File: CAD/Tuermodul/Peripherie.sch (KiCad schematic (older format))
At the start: 63 parts, among them J201 Conn_02x20_Odd_Even, Q205 Q_NPN_CBE, Q206 Q_NPN_CBE, Q207 Q_NPN_CBE, Q208 Q_NPN_CBE, Q209 Q_PMOS_GDS, Q210 Q_PMOS_GDS, Q211 Q_PMOS_GDS, Q212 Q_PMOS_GDS, Q213 Q_NPN_CBE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

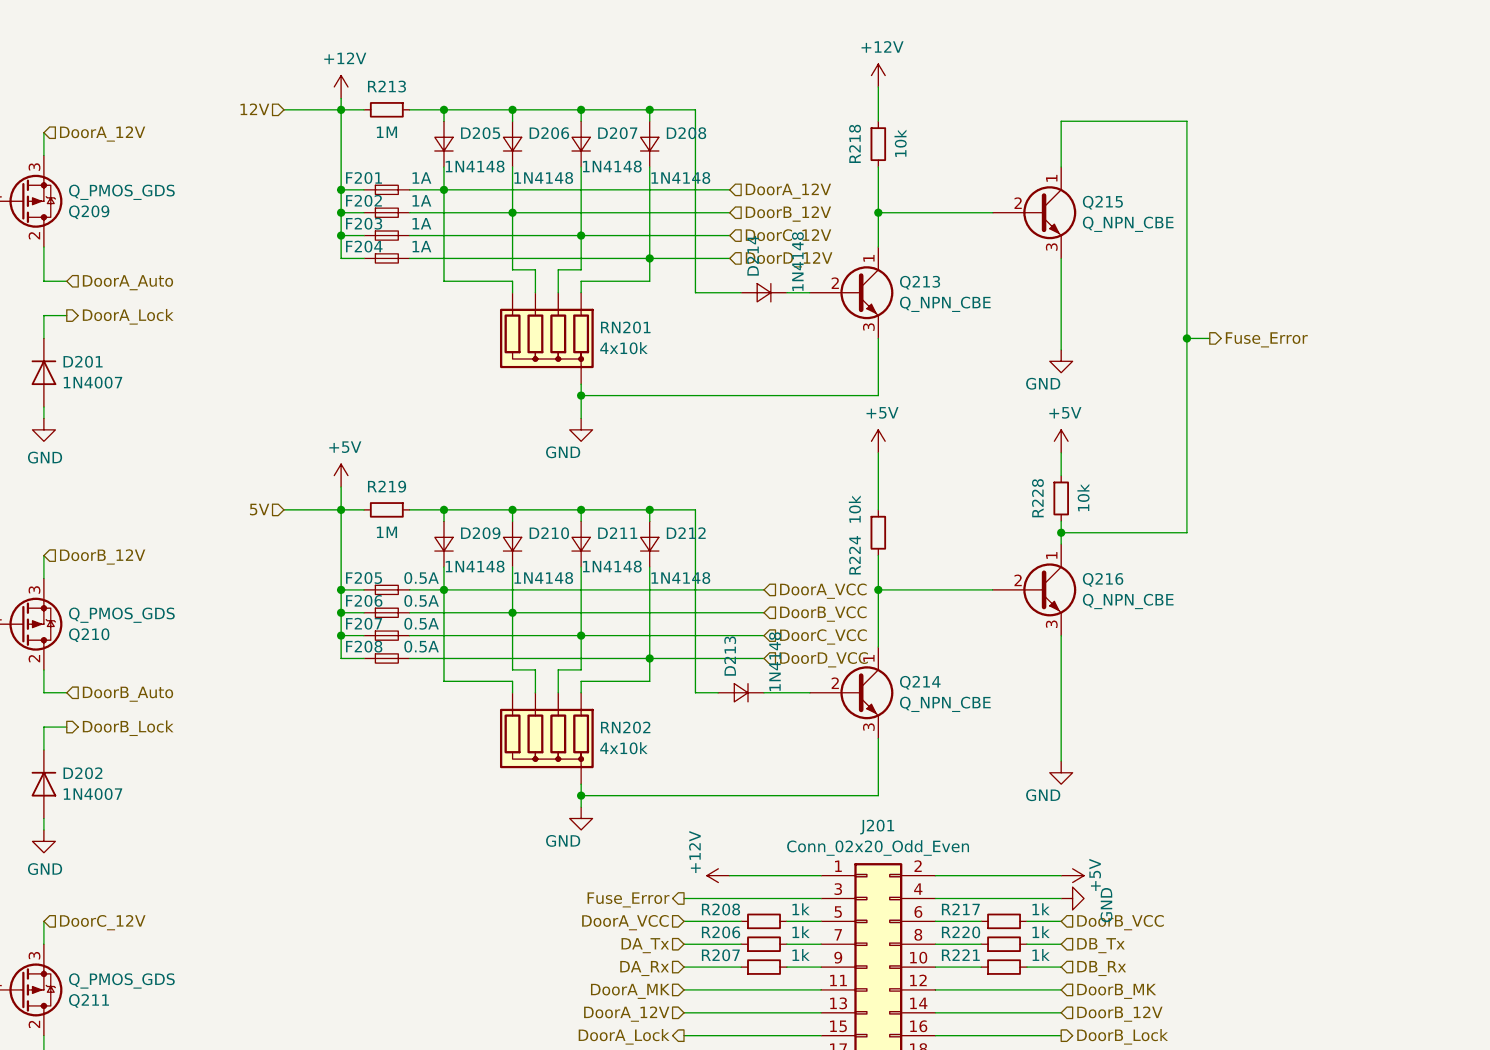
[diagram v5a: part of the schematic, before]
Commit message: -mod: Änderungen aus Review in Schaltplan und Layout
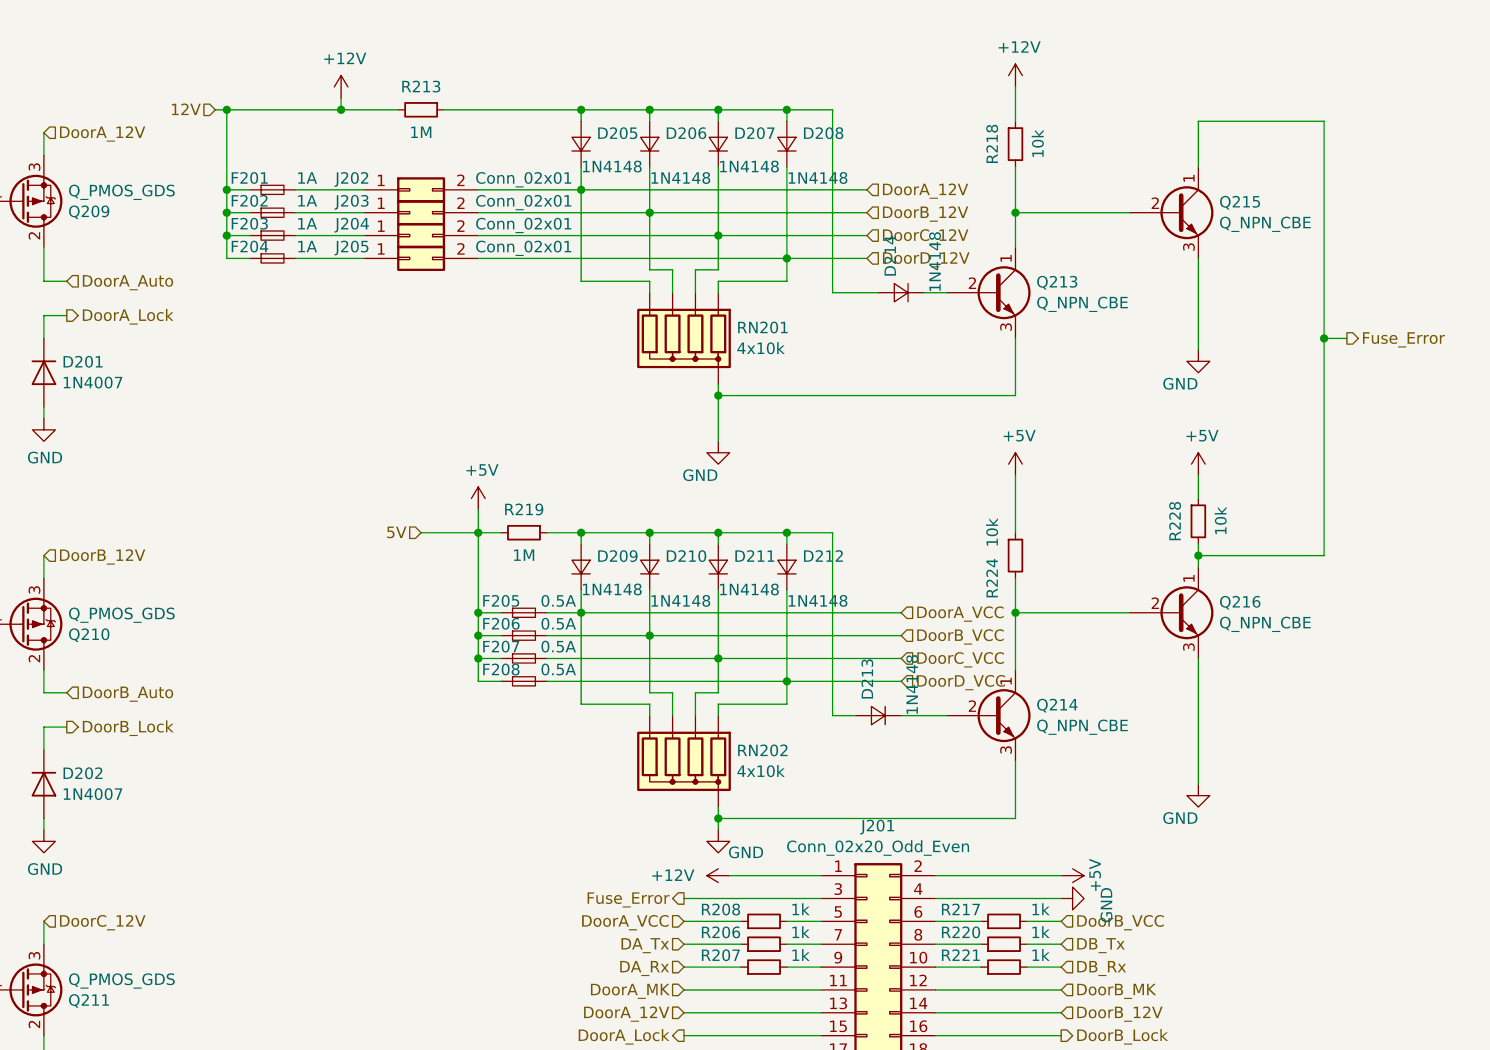
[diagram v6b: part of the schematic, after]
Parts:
- added J202, J203, J204, J205: Conn_02x01, Connector_PinHeader_2.54mm:PinHeader_2x01_P2.54mm_Vertical, symbol Connector_Generic:Conn_02x01
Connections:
- net DoorA_12V: now also J202.2 (Pin_2); no longer F201.2
- net DoorB_12V: now also J203.2 (Pin_2); no longer F202.2
- net DoorC_12V: now also J204.2 (Pin_2); no longer F203.2
- net DoorD_12V: now also J205.2 (Pin_2); no longer F204.2
- new net: F201.2, J202.1 (Pin_1)
- new net: F202.2, J203.1 (Pin_1)
- new net: F203.2, J204.1 (Pin_1)
- new net: F204.2, J205.1 (Pin_1)
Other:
- moved on the sheet: D205, D206, D207, D208, D209, D210, D211, D212, D213, D214, F201, F202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
